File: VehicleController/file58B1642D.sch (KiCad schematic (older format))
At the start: 23 parts, among them Q4 Q_NMOS_GDS, Q5 PC_FET, U13 RI-0505S, U14 ISO1540, U15 PC_RLY, U16 MCR_Shtdwn, U17 MCL_Shtdwn, U18 TCMT1103, U19 MCP47FEBX2, U20 MX123_56

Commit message: VCU Changes post ESF
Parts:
- removed unit 2 of U20
- added U22: OPTO-TRANSISTOR-4, symbol OPTO-TRANSISTOR-4
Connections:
- net labels added: F_L1, F_L2, F_R1, F_R2
- wire segments 149 -> 137
- no-connect marks 1 -> 5
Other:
- moved on the sheet: Q4, R22, R25, R26, U18

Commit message: Add reset switch on VCU
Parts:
- removed U20: MX123_56, UNCAMotorsports:MX123_56, symbol MX123_56
- added J3: CONN_02X12, symbol CONN_02X12
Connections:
- wire segments 137 -> 173
- no-connect marks 5 -> 1

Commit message: Add BTS4130's for 12v and 5v outputs
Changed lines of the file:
@@
 	7850 5750 7750 5750
 Wire Wire Line
-	7850 5450 7850 5500
-Wire Wire Line
-	7850 5500 7850 5750
-Wire Wire Line
-	7850 5500 8000 5500
-Wire Wire Line
-	8000 5500 8300 5500
+	7850 5450 7850 5750
+Wire Wire Line
+	7850 5500 8300 5500
 Wire Wire Line
 	8000 5500 8000 5550
 Connection ~ 7850 5500
 Wire Wire Line
-	7750 5850 8000 5850
-Wire Wire Line
-	8000 5850 8850 5850
+	7750 5850 8850 5850
 Wire Wire Line
 	8000 5850 8000 5750
 Connection ~ 8000 5850
 Wire Wire Line
-	7750 5950 8300 5950
-Wire Wire Line
-	8300 5950 8850 5950
+	7750 5950 8850 5950
 Wire Wire Line
 	8300 5500 8300 5550
@@
 	7850 4450 7850 4550
 Wire Wire Line
-	7750 4550 7850 4550
-Wire Wire Line
-	7850 4550 8000 4550
+	7750 4550 8000 4550
 Wire Wire Line
 	7750 4650 7850 4650
@@
 	12500 5700 12900 5700
 Wire Wire Line
-	7600 7900 7700 7900
-Wire Wire Line
-	7700 7900 8250 7900
+	7600 7900 8250 7900
 Wire Wire Line
 	7700 7800 7700 7900
@@
 	6750 4800 6750 4650
 Wire Wire Line
-	6050 5850 6300 5850
-Wire Wire Line
-	6300 5850 6850 5850
-Wire Wire Line
-	6050 5950 6600 5950
-Wire Wire Line
-	6600 5950 6850 5950
-Wire Wire Line
-	6750 5400 6750 5500
-Wire Wire Line
-	6750 5500 6750 5750
+	6050 5850 6850 5850
+Wire Wire Line
+	6050 5950 6850 5950
+Wire Wire Line
+	6750 5400 6750 5750
 Wire Wire Line
 	7500 3100 7500 3200
@@
 	7500 3200 8100 3200
 Wire Wire Line
-	7500 2650 8350 2650
-Wire Wire Line
-	8350 2650 8750 2650
+	7500 2650 8750 2650
 Wire Wire Line
 	8350 2650 8350 3350
@@
 	6300 5550 6300 5500
 Wire Wire Line
-	6300 5500 6600 5500
-Wire Wire Line
-	6600 5500 6750 5500
+	6300 5500 6750 5500
 Connection ~ 6750 5500
 Wire Wire Line
@@
 Connection ~ 6600 5950
 Wire Wire Line
-	12150 3450 12300 3450
-Wire Wire Line
-	12300 3450 12650 3450
+	12150 3450 12650 3450
 Wire Wire Line
 	12650 4050 12150 4050
@@
 	11650 4550 11550 4550
 Wire Wire Line
-	11550 4450 11550 4550
-Wire Wire Line
-	11550 4550 11550 4650
+	11550 4450 11550 4650
 Wire Wire Line
 	12150 4150 12650 4150
 Wire Wire Line
-	11100 3450 11500 3450
-Wire Wire Line
-	11500 3450 11650 3450
+	11100 3450 11650 3450
 Wire Wire Line
 	11100 4050 11650 4050
@@
 	12150 4550 12250 4550
 Wire Wire Line
-	12250 4450 12250 4550
-Wire Wire Line
-	12250 4550 12250 4650
+	12250 4450 12250 4650
 Wire Wire Line
 	11650 4150 11100 4150
 Wire Wire Line
-	7200 750  7200 950
-Wire Wire Line
-	7200 950  7200 1000
-Wire Wire Line
-	7200 1400 7200 1450
-Wire Wire Line
-	7200 1450 7200 1500
+	7200 750  7200 1000
+Wire Wire Line
+	7200 1400 7200 1500
 Wire Wire Line
 	7450 1400 7450 1550
@@
 	8450 1550 8700 1550
 Wire Wire Line
-	7450 1550 7850 1550
-Wire Wire Line
-	7850 1550 8150 1550
+	7450 1550 8150 1550
 Wire Wire Line
 	8050 850  7850 850
 Connection ~ 7850 1550
 Wire Wire Line
-	6850 6800 6850 6950
-Wire Wire Line
-	6850 6950 6850 7050
+	6850 6800 6850 7050
 Wire Wire Line
 	6850 7750 6850 7900
@@
 	6450 7200 6450 7250
 Wire Wire Line
-	6200 7250 6450 7250
-Wire Wire Line
-	6450 7250 6550 7250
+	6200 7250 6550 7250
 Wire Wire Line
 	6450 7000 6450 6950
@@
 Connection ~ 7200 1450
 Wire Wire Line
-	7200 1900 7200 2000
-Wire Wire Line
-	7200 2000 7200 2100
+	7200 1900 7200 2100
 Wire Wire Line
 	6850 1750 6850 1700
 Wire Wire Line
-	6550 1700 6850 1700
-Wire Wire Line
-	6850 1700 6900 1700
+	6550 1700 6900 1700
 Wire Wire Line
 	6850 1950 6850 2000
@@
 Connection ~ 7200 950
 Wire Wire Line
-	11500 3450 11500 3550
-Wire Wire Line
-	11500 3550 11500 3650
-Wire Wire Line
-	11500 3650 11500 3750
-Wire Wire Line
-	11500 3750 11500 3850
-Wire Wire Line
-	11500 3850 11500 3950
+	11500 3450 11500 3950
 Connection ~ 11500 3550
 Connection ~ 11500 3450
@@
 Connection ~ 11500 3750
 Wire Wire Line
-	12300 3450 12300 3550
-Wire Wire Line
-	12300 3550 12300 3650
-Wire Wire Line
-	12300 3650 12300 3750
-Wire Wire Line
-	12300 3750 12300 3850
-Wire Wire Line
-	12300 3850 12300 3950
+	12300 3450 12300 3950
 Connection ~ 12300 3550
 Connection ~ 12300 3450
@@
 	7600 8850 7700 8850
 Wire Wire Line
-	7700 8850 7700 9250
-Wire Wire Line
-	7700 9250 7700 9650
-Wire Wire Line
-	7700 9650 7700 10050
-Wire Wire Line
-	7700 10050 7700 10150
+	7700 8850 7700 10150
 Wire Wire Line
 	7600 9250 7700 9250
@@
 	7000 8850 6900 8850
 Wire Wire Line
-	6900 8850 6900 9250
-Wire Wire Line
-	6900 9250 6900 9650
-Wire Wire Line
-	6900 9650 6900 10050
-Wire Wire Line
-	6900 10050 6900 10150
+	6900 8850 6900 10150
 Wire Wire Line
 	7000 10050 6900 10050

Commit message: More updates prior to finalizing design
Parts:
- added J?: CONN_01X03, symbol CONN_01X03
- added R44: 470, Resistors_SMD:R_0805_HandSoldering, symbol R_Small
- added U24, U25: TCMT1103, UNCAMotorsports:SSOP-4, symbol TCMT1103
- renumbered D11 to D13, D12 to D14, D13 to D15, D14 to D16, J3 to J4, R21 to R35, R22 to R36, R23 to R37, R24 to R38, R25 to R39, R26 to R40, R27 to R41, R28 to R42, R29 to R43, U13 to U16, U14 to U17, U22 to U19, U15 to U20, U16 to U21, U17 to U22, U19 to U23
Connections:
- net CONTACT_L: now also U24.4
- net CONTACT_R: now also U25.4
- net GND: now also U24.2, U25.2
- net GNDA: now also J?.3 (P3), U24.3, U25.3
- net HV_BATT+: now also J?.1 (P1)
- net TS+: now also J?.2 (P2)
- new net: R44.1, U24.1, U25.1
- new net MC_OVERRIDE: R44.2
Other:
- moved on the sheet: D16, Q4, R35, R36, R37, R39, R41, R42, R43, U16, U17, U21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

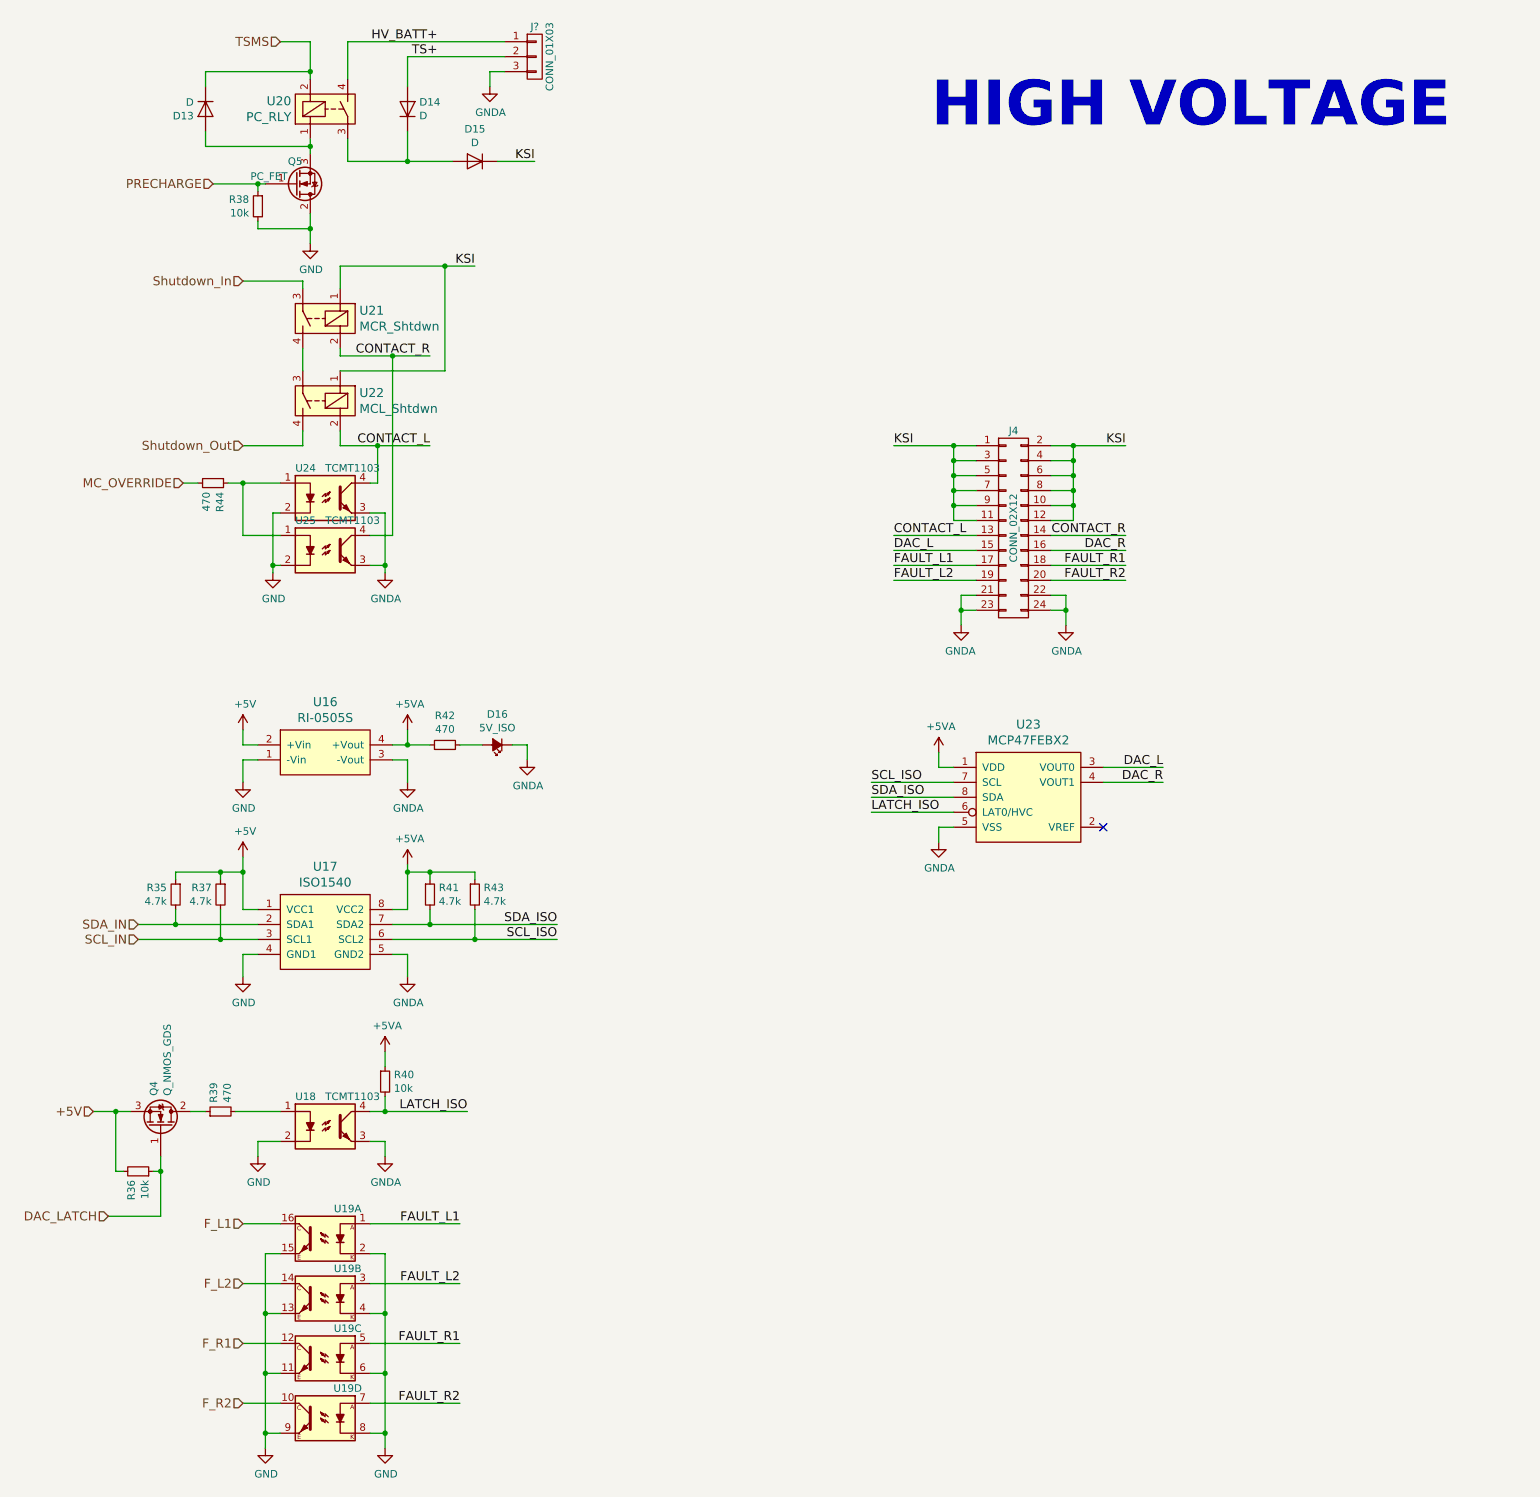
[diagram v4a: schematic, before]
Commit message: VCU changes to precharge and MC Override
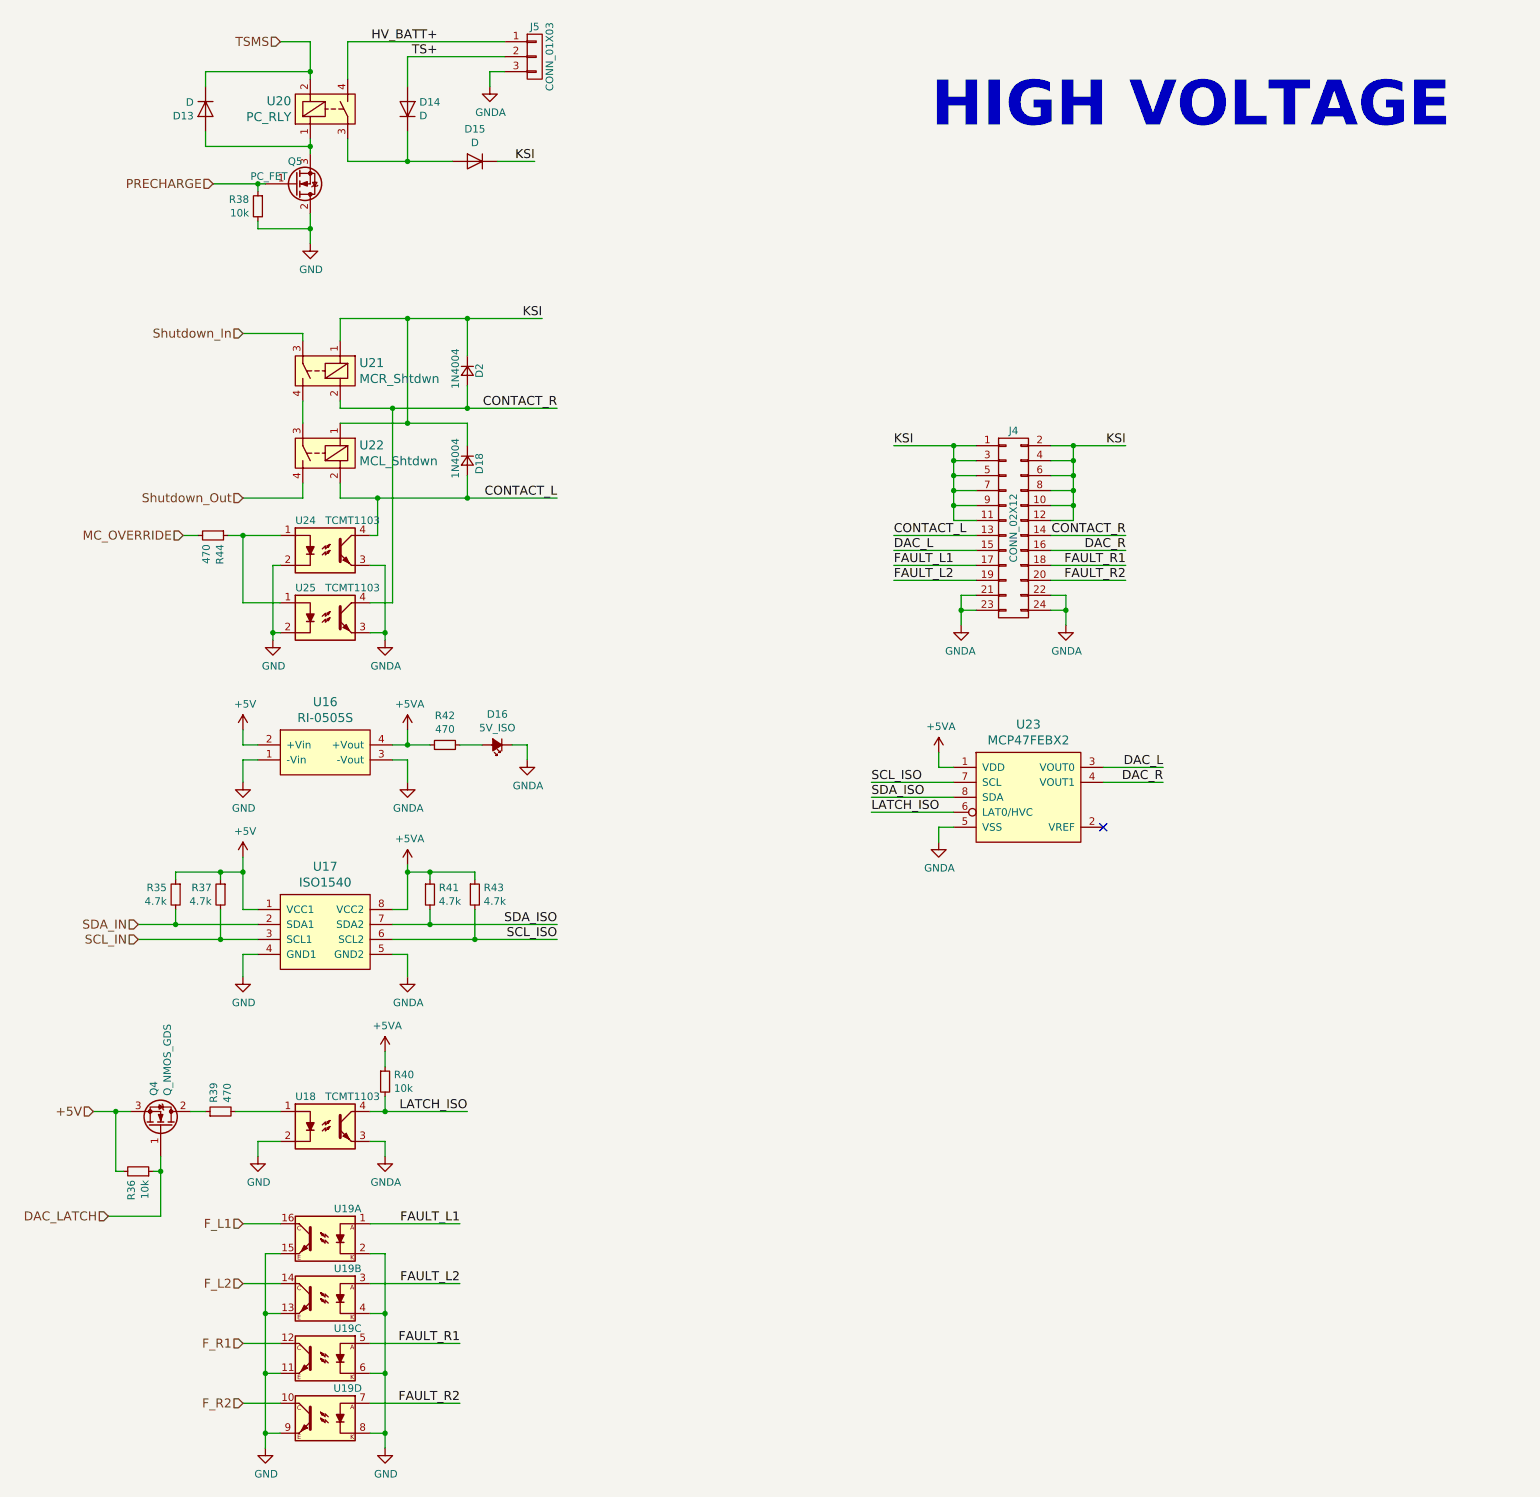
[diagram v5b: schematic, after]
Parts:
- added D18, D2: 1N4004, symbol D_Small
- gave numbers to parts that had none: 1
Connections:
- net CONTACT_L: now also D18.2 (A)
- net CONTACT_R: now also D2.2 (A)
- net KSI: now also D18.1 (K), D2.1 (K)
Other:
- moved on the sheet: R44, U21, U22, U24, U25

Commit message: Fix Motor Controller Override circuit, better net names
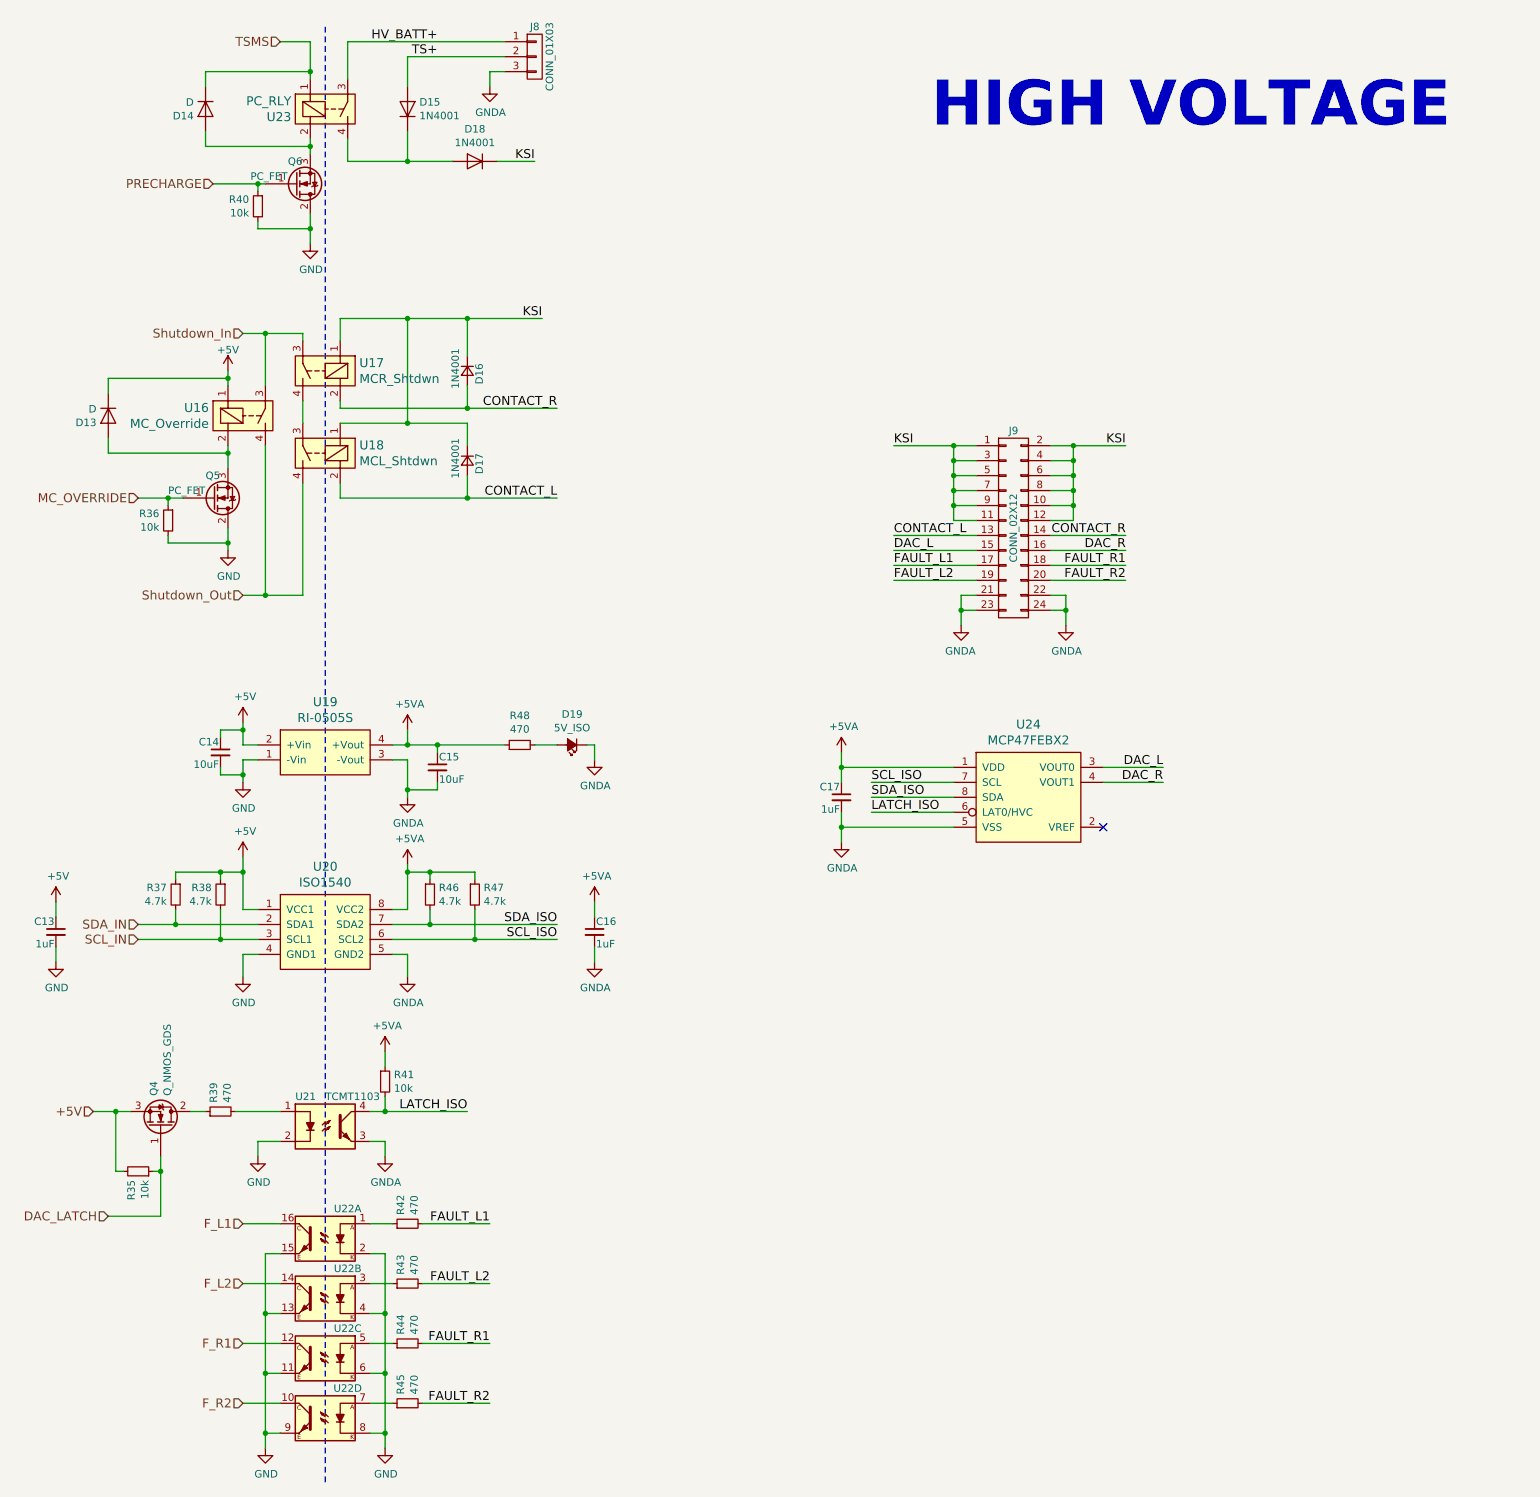
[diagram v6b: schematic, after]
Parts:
- removed U24, U25: TCMT1103, UNCAMotorsports:SSOP-4, symbol TCMT1103
- added C13, C16, C17: 1uF, Capacitors_SMD:C_0805_HandSoldering, symbol C_Small
- added C14, C15: 10uF, Capacitors_SMD:C_0805_HandSoldering, symbol C_Small
- added D13: D, Diodes_SMD:SMA_Handsoldering, symbol D
- added Q5: PC_FET, TO_SOT_Packages_SMD:SOT-23_Handsoldering, symbol Q_NMOS_GDS
- added R36: 10k, Resistors_SMD:R_0805_HandSoldering, symbol R_Small
- added R42, R43, R45: 470, Resistors_SMD:R_0805_HandSoldering, symbol R_Small
- added U16: MC_Override, UNCAMotorsports:ALE1PB48, symbol Relay_SPST
- D15: renamed from D14; value D -> 1N4001
- D16: renamed from D2; value 1N4004 -> 1N4001
- D17: renamed from D18; value 1N4004 -> 1N4001
- D18: renamed from D15; value D -> 1N4001
- renumbered D13 to D14, D16 to D19, J5 to J8, J4 to J9, Q5 to Q6, R36 to R35, R35 to R37, R37 to R38, R38 to R40, R40 to R41, R41 to R46, R43 to R47, R42 to R48, U21 to U17, U22 to U18, U16 to U19, U17 to U20, U18 to U21, U19 to U22, U20 to U23, U23 to U24
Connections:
- net +5V: now also C13.1, C14.1, D13.1 (K), U16.1
- net +5VA: now also C15.1, C16.1, C17.1
- net FAULT_L1: now also R42.2; no longer U22.1
- net FAULT_L2: now also R43.2; no longer U22.3
- net FAULT_R1: now also R44.2; no longer U22.5
- net FAULT_R2: now also R45.2; no longer U22.7
- net GND: now also C13.2, C14.2, Q5.2 (D), R36.2
- net GNDA: now also C15.2, C16.2, C17.2
- net HV_BATT+: now also U23.3; no longer U23.4
- net MC_OVERRIDE: now also Q5.1 (G), R36.1; no longer R44.2
- net Shutdown_In: now also U16.3
- net Shutdown_Out: now also U16.4
- net TSMS: now also U23.1; no longer U23.2
- net at D14.2 (A), Q6.3 (S): now also U23.2; no longer U23.1
- net at D15.1 (K), D18.2 (A): now also U23.4; no longer U23.3
- net at R44.1: now also U22.5
- new net: R42.1, U22.1
- new net: R43.1, U22.3
- new net: R45.1, U22.7
- new net: D13.2 (A), Q5.3 (S), U16.2
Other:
- moved on the sheet: D19, R48
